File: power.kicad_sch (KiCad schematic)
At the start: 9 parts, among them J1 Conn_01x02, U1 MC34063AD

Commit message: Stuff
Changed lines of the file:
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@@
   (junction (at 172.72 77.47) (diameter 0) (color 0 0 0 0)
-  )
-  (junction (at 187.96 113.03) (diameter 0) (color 0 0 0 0)
   )
   (junction (at 187.96 77.47) (diameter 0) (color 0 0 0 0)
@@
     (stroke (width 0) (type default))
   )
-  (wire (pts (xy 187.96 113.03) (xy 199.39 113.03))
-    (stroke (width 0) (type default))
-  )
   (wire (pts (xy 120.65 77.47) (xy 120.65 105.41))
     (stroke (width 0) (type default))
@@
     (stroke (width 0) (type default))
   )
-  (wire (pts (xy 199.39 90.17) (xy 199.39 113.03))
-    (stroke (width 0) (type default))
-  )
   (wire (pts (xy 135.89 77.47) (xy 161.29 77.47))
     (stroke (width 0) (type default))
   )
-  (wire (pts (xy 199.39 77.47) (xy 199.39 82.55))
-    (stroke (width 0) (type default))
-  )

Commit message: changes
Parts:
- removed C2: 1.5n, Capacitor_SMD:C_0603_1608Metric, symbol Device:C
- removed U1: MC34063AD, Package_SO:SOIC-8_3.9x4.9mm_P1.27mm, symbol Regulator_Switching:MC34063AD
- added C12, C2: C, Capacitor_SMD:CP_Elec_6.3x7.7, symbol Device:C_Polarized
- added U2: MIC2288, Package_SO:TSOP-5_1.65x3.05mm_P0.95mm, symbol custom_symbols:MIC2288
- J2: renamed from J1; footprint Connector_PinHeader_2.54mm:PinHeader_1x02_P2.54mm_Horizontal -> custom:SAMTEC_TSM-102-01-L-SH; symbol Connector_Generic:Conn_01x02 -> custom_symbols:TSM-102-01-L-SH; MANUFACTURER (none) -> Samtec; PARTREV (none) -> R; STANDARD (none) -> Manufacturer Recommendations; now in the parts list
- L1: footprint Inductor_SMD:L_Taiyo-Yuden_MD-4040 -> custom:IND_357100_WRE
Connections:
- net +BATT: now also J2.02, U2.5 (VIN); no longer J2.2 (Pin_2)
- net GND: now also J2.01, C12.2, C2.2, U2.2 (GND); no longer J2.1 (Pin_1)
- net Vdrive: now also C12.1, C2.1
- net at D3.2 (A), L1.2: now also U2.1 (SW)
- net at RV1.2: now also U2.3 (FB)
- new net EN: U2.4 (EN)
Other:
- moved on the sheet: J2, RV1

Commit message: Shrunkified
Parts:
- removed C2: C, Capacitor_SMD:CP_Elec_6.3x7.7, symbol Device:C_Polarized
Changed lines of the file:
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@@
     (effects (font (size 1.27 1.27)) (justify right))
-  )
-  (symbol (lib_id "Device:C_Polarized") (at 217.17 96.52 0) (unit 1)
-    (in_bom yes) (on_board yes) (dnp no) (fields_autoplaced)
-    (property "Reference" "C2" (at 220.98 94.361 0)
-      (effects (font (size 1.27 1.27)) (justify left))
-    )
-    (property "Value" "C" (at 220.98 96.901 0)
-      (effects (font (size 1.27 1.27)) (justify left))
-    )
-    (property "Footprint" "Capacitor_SMD:CP_Elec_6.3x7.7" (at 218.1352 100.33 0)
-      (effects (font (size 1.27 1.27)) hide)
-    )
-    (property "Datasheet" "~" (at 217.17 96.52 0)
-      (effects (font (size 1.27 1.27)) hide)
-    )
-    (pin "1")
-    (pin "2")
-    (instances
-      (project "locator_beacon"
-        (path "/2e37f9ca-1f81-48a3-bbbb-9eab5c177622/45852106-87c2-4e1d-b1b1-72b985aa268b"
-          (reference "C2") (unit 1)
-        )
-      )
-    )
   )
   (symbol (lib_id "custom_symbols:MIC2288") (at 151.13 93.98 0) (unit 1)

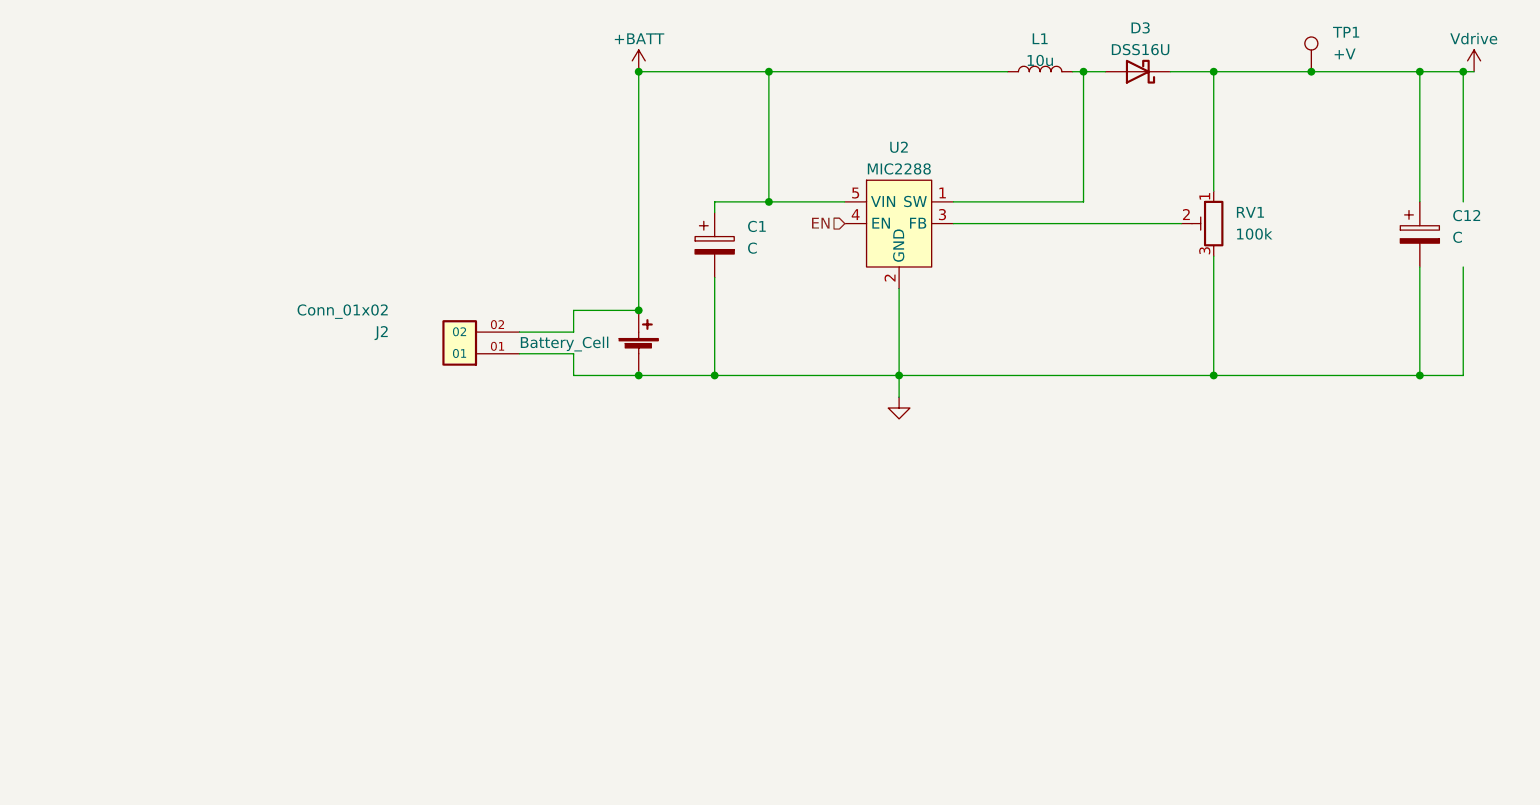
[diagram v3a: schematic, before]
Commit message: Separate +12 and boost
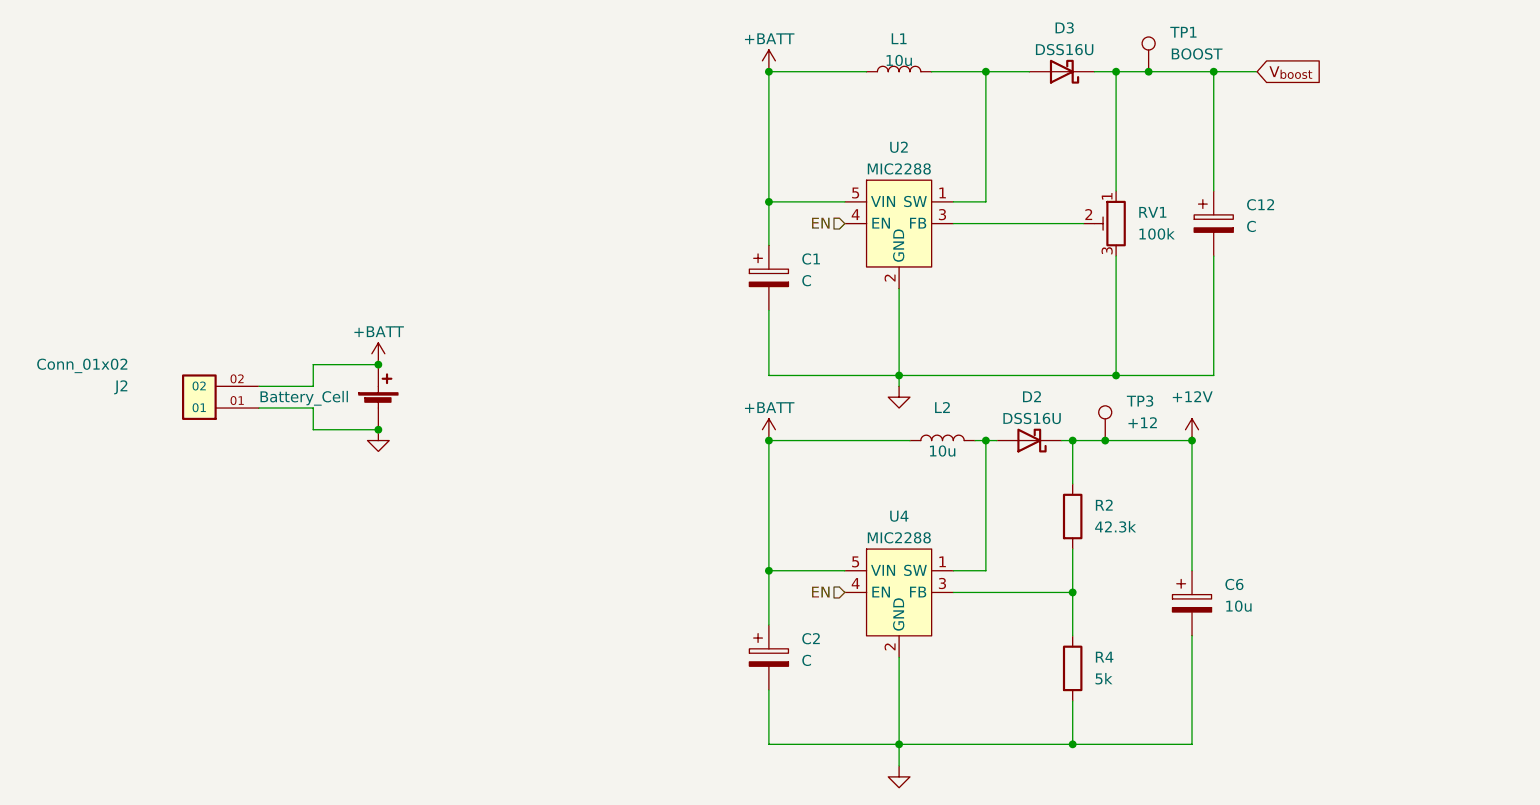
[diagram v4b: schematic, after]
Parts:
- added C2: C, Capacitor_SMD:C_0603_1608Metric, symbol Device:C_Polarized
- added C6: 10u, Capacitor_SMD:C_0603_1608Metric, symbol Device:C_Polarized
- added D2: DSS16U, Diode_SMD:D_SOD-123, symbol Diode:B120-E3
- added L2: 10u, custom:IND_357100_WRE, symbol Device:L
- added R2: 42.3k, Resistor_SMD:R_0603_1608Metric, symbol Device:R
- added R4: 5k, Resistor_SMD:R_0603_1608Metric, symbol Device:R
- added TP3: +12, TestPoint:TestPoint_Pad_D1.0mm, symbol Connector:TestPoint
- added U4: MIC2288, Package_SO:TSOP-5_1.65x3.05mm_P0.95mm, symbol custom_symbols:MIC2288
- TP1: value +V -> BOOST
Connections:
- net +BATT: now also C2.1, L2.1, U4.5 (VIN)
- net EN: now also U4.4 (EN)
- net GND: now also C2.2, C6.2, R4.2, U4.2 (GND)
- net Vdrive renamed V_{boost}
- new net: R2.2, R4.1, U4.3 (FB)
- new net: D2.2 (A), L2.2, U4.1 (SW)
- new net +12V: C6.1, D2.1 (K), R2.1, TP3.1
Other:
- moved on the sheet: C1, C12, D3, J2, L1, RV1, TP1
